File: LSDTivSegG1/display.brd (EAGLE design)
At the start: 150 x 100 mm, 95 parts, among them IC1 MEGA8-P, IC2 MAX232, IC3 PCF8574P, IC4 PCF8574P, IC5 PCF8574P, IC6 PCF8574P

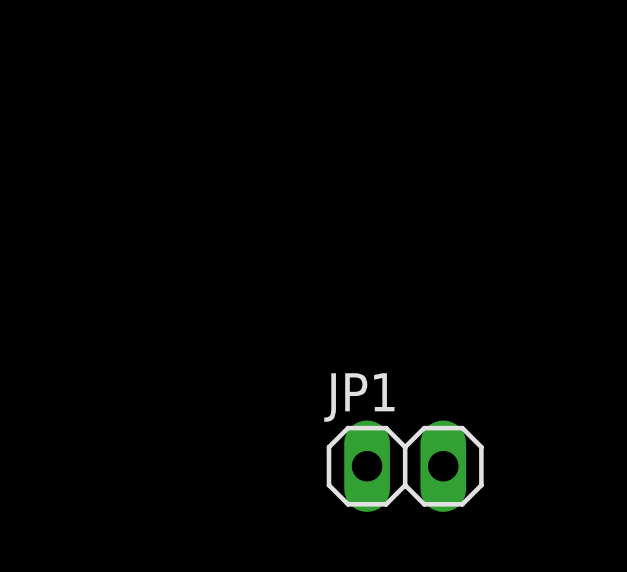
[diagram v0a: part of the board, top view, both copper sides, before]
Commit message: added RS232 crossing pinhead
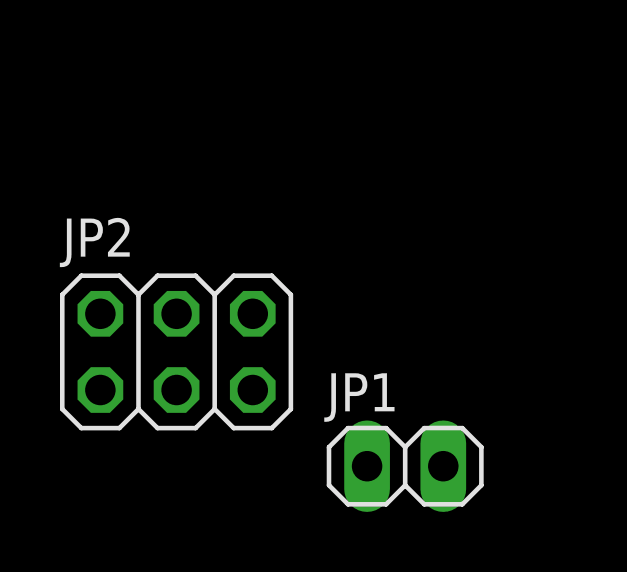
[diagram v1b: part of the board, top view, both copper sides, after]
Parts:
- added JP2: (no value), pinhead:2X03
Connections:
- new net RS232RX_CON: JP2.3, X1.2
- new net RS232TX_CON: JP2.4, X1.3
- net RS232RX: now also JP2.1, JP2.6; no longer X1.4
- net RS232TX: now also JP2.2, JP2.5; no longer X1.3
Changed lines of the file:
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@@
 <element name="U$2" library="lsd2016" package="BOARD" value="PCB" x="0" y="0"/>
 <element name="JP1" library="pinhead" library_urn="urn:adsk.eagle:library:325" package="1X02" package3d_urn="urn:adsk.eagle:package:22435/2" value="" x="-132.08" y="-5.08"/>
+<element name="JP2" library="pinhead" library_urn="urn:adsk.eagle:library:325" package="2X03" package3d_urn="urn:adsk.eagle:package:22462/2" value="" x="-139.7" y="-1.27"/>
 </elements>
 <signals>
@@
 </signal>
 <signal name="RS232TX">
-<contactref element="X1" pad="3"/>
 <contactref element="IC2" pad="13"/>
-<wire x1="-121.92" y1="96.52" x2="-29.21" y2="67.31" width="0" layer="19" extent="1-1"/>
+<contactref element="JP2" pad="5"/>
+<contactref element="JP2" pad="2"/>
+<wire x1="-137.16" y1="-2.54" x2="-142.24" y2="0" width="0" layer="19" extent="1-1"/>
+<wire x1="-121.92" y1="96.52" x2="-142.24" y2="0" width="0" layer="19" extent="1-1"/>
 </signal>
 <signal name="RS232RX">
-<contactref element="X1" pad="4"/>
 <contactref element="IC2" pad="14"/>
-<wire x1="-124.46" y1="96.52" x2="-26.4668" y2="67.31" width="0" layer="19" extent="1-1"/>
+<contactref element="JP2" pad="1"/>
+<contactref element="JP2" pad="6"/>
+<wire x1="-137.16" y1="0" x2="-142.24" y2="-2.54" width="0" layer="19" extent="1-1"/>
+<wire x1="-124.46" y1="96.52" x2="-137.16" y2="0" width="0" layer="19" extent="1-1"/>
 </signal>
 <signal name="N$1">
@@
 <wire x1="-119.38" y1="124.46" x2="-116.84" y2="88.9" width="0" layer="19" extent="1-1"/>
 </signal>
+<signal name="RS232RX_CON">
+<contactref element="X1" pad="2"/>
+<contactref element="JP2" pad="3"/>
+<wire x1="-31.9532" y1="67.31" x2="-139.7" y2="-2.54" width="0" layer="19" extent="1-1"/>
+</signal>
+<signal name="RS232TX_CON">
+<contactref element="X1" pad="3"/>
+<contactref element="JP2" pad="4"/>
+<wire x1="-29.21" y1="67.31" x2="-139.7" y2="0" width="0" layer="19" extent="1-1"/>
+</signal>
 </signals>

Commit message: added supply pins to max232
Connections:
- removed net VCC: IC2.16
- net +5V: now also IC2.16; no longer C6.-
- net GND: now also C6.-
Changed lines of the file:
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@@
 </elements>
 <signals>
-<signal name="VCC">
-<contactref element="IC2" pad="16"/>
-</signal>
 <signal name="GND">
-<contactref element="IC2" pad="15"/>
 <contactref element="C3" pad="2"/>
 <contactref element="C2" pad="2"/>
@@
 <vertex x="0" y="0"/>
 </polygon>
-<contactref element="C7" pad="+"/>
 <contactref element="SV1" pad="4"/>
 <contactref element="SV1" pad="6"/>
 <contactref element="SV1" pad="8"/>
 <contactref element="SV1" pad="10"/>
+<contactref element="C7" pad="+"/>
+<contactref element="C6" pad="-"/>
+<contactref element="IC2" pad="15"/>
 <wire x1="72.39" y1="54.61" x2="69.85" y2="62.23" width="0" layer="19" extent="1-1"/>
 <wire x1="68.58" y1="50.8" x2="72.39" y2="54.61" width="0" layer="19" extent="1-1"/>
@@
 <wire x1="-85.6488" y1="103.8606" x2="-81.9912" y2="103.8606" width="0" layer="19" extent="1-1"/>
 <wire x1="-92.1512" y1="103.8606" x2="-85.6488" y2="103.8606" width="0" layer="19" extent="1-1"/>
+<wire x1="-110.49" y1="124.46" x2="-92.1512" y2="103.8606" width="0" layer="19" extent="1-1"/>
+<wire x1="-102.87" y1="130.81" x2="-110.49" y2="124.46" width="0" layer="19" extent="1-1"/>
+<wire x1="-121.92" y1="124.46" x2="-110.49" y2="124.46" width="0" layer="19" extent="1-1"/>
 <wire x1="-127" y1="96.52" x2="-100.33" y2="88.9" width="0" layer="19" extent="1-1"/>
 <wire x1="-21.59" y1="132.08" x2="-21.0312" y2="103.8606" width="0" layer="19" extent="1-1"/>
@@
 <wire x1="-34.29" y1="132.08" x2="-27.94" y2="132.08" width="0" layer="19" extent="1-1"/>
 <wire x1="-40.64" y1="132.08" x2="-34.29" y2="132.08" width="0" layer="19" extent="1-1"/>
-<wire x1="-121.92" y1="124.46" x2="-127" y2="96.52" width="0" layer="19" extent="1-1"/>
-<wire x1="-102.87" y1="130.81" x2="-121.92" y2="124.46" width="0" layer="19" extent="1-1"/>
 <wire x1="-101.6" y1="58.42" x2="-100.33" y2="88.9" width="0" layer="19" extent="1-1"/>
 </signal>
@@
 <contactref element="R3" pad="1"/>
 <contactref element="R5" pad="2"/>
-<contactref element="C6" pad="-"/>
 <contactref element="R12" pad="2"/>
 <contactref element="R13" pad="2"/>
@@
 <contactref element="JP1" pad="2"/>
 <contactref element="SV1" pad="2"/>
+<contactref element="IC2" pad="16"/>
 <wire x1="72.39" y1="62.23" x2="74.93" y2="62.23" width="0" layer="19" extent="1-1"/>
 <wire x1="69.85" y1="54.61" x2="72.39" y2="62.23" width="0" layer="19" extent="1-1"/>
@@
 <wire x1="-105.41" y1="88.9" x2="-102.87" y2="88.9" width="0" layer="19" extent="1-1"/>
 <wire x1="-105.41" y1="96.52" x2="-105.41" y2="88.9" width="0" layer="19" extent="1-1"/>
+<wire x1="-129.54" y1="96.52" x2="-105.41" y2="96.52" width="0" layer="19" extent="1-1"/>
 <wire x1="-99.06" y1="58.42" x2="-72.39" y2="67.31" width="0" layer="19" extent="1-1"/>
-<wire x1="-110.49" y1="124.46" x2="-105.41" y2="96.52" width="0" layer="19" extent="1-1"/>
-<wire x1="-113.03" y1="130.81" x2="-110.49" y2="124.46" width="0" layer="19" extent="1-1"/>
-<wire x1="-114.3" y1="137.16" x2="-113.03" y2="130.81" width="0" layer="19" extent="1-1"/>
-<wire x1="-114.3" y1="142.24" x2="-114.3" y2="137.16" width="0" layer="19" extent="1-1"/>
-<wire x1="-102.87" y1="130.81" x2="-110.49" y2="124.46" width="0" layer="19" extent="1-1"/>
+<wire x1="-102.87" y1="130.81" x2="-105.41" y2="96.52" width="0" layer="19" extent="1-1"/>
 <wire x1="-104.14" y1="137.16" x2="-102.87" y2="130.81" width="0" layer="19" extent="1-1"/>
 <wire x1="-104.14" y1="142.24" x2="-104.14" y2="137.16" width="0" layer="19" extent="1-1"/>
@@
 <wire x1="-12.7" y1="147.32" x2="-22.86" y2="147.32" width="0" layer="19" extent="1-1"/>
 <wire x1="-12.7" y1="142.24" x2="-12.7" y2="147.32" width="0" layer="19" extent="1-1"/>
+<wire x1="-114.3" y1="142.24" x2="-104.14" y2="142.24" width="0" layer="19" extent="1-1"/>
+<wire x1="-114.3" y1="137.16" x2="-114.3" y2="142.24" width="0" layer="19" extent="1-1"/>
+<wire x1="-113.03" y1="130.81" x2="-114.3" y2="137.16" width="0" layer="19" extent="1-1"/>
 <wire x1="-124.46" y1="142.24" x2="-114.3" y2="142.24" width="0" layer="19" extent="1-1"/>
 <wire x1="-124.46" y1="137.16" x2="-124.46" y2="142.24" width="0" layer="19" extent="1-1"/>
@@
 <wire x1="-92.71" y1="124.46" x2="-124.46" y2="88.9" width="0" layer="19" extent="1-1"/>
 </signal>
-<signal name="N$7">
-<contactref element="IC2" pad="2"/>
-<contactref element="C6" pad="+"/>
-<wire x1="-113.03" y1="124.46" x2="-127" y2="88.9" width="0" layer="19" extent="1-1"/>
-</signal>
 <signal name="N$15">
 <contactref element="R12" pad="1"/>
@@
 <wire x1="-25.0952" y1="69.85" x2="-133.35" y2="-5.08" width="0" layer="19" extent="1-1"/>
 </signal>
+<signal name="RS232RX_CON">
+<contactref element="X1" pad="2"/>
+<contactref element="JP2" pad="3"/>
+<wire x1="-31.9532" y1="67.31" x2="-139.7" y2="-2.54" width="0" layer="19" extent="1-1"/>
+</signal>
+<signal name="RS232TX_CON">
+<contactref element="X1" pad="3"/>
+<contactref element="JP2" pad="4"/>
+<wire x1="-29.21" y1="67.31" x2="-139.7" y2="0" width="0" layer="19" extent="1-1"/>
+</signal>
+<signal name="N$7">
+<contactref element="IC2" pad="2"/>
+<contactref element="C6" pad="+"/>
+<wire x1="-113.03" y1="124.46" x2="-127" y2="88.9" width="0" layer="19" extent="1-1"/>
+</signal>
 <signal name="N$8">
 <contactref element="IC2" pad="6"/>
@@
 <wire x1="-119.38" y1="124.46" x2="-116.84" y2="88.9" width="0" layer="19" extent="1-1"/>
 </signal>
-<signal name="RS232RX_CON">
-<contactref element="X1" pad="2"/>
-<contactref element="JP2" pad="3"/>
-<wire x1="-31.9532" y1="67.31" x2="-139.7" y2="-2.54" width="0" layer="19" extent="1-1"/>
-</signal>
-<signal name="RS232TX_CON">
-<contactref element="X1" pad="3"/>
-<contactref element="JP2" pad="4"/>
-<wire x1="-29.21" y1="67.31" x2="-139.7" y2="0" width="0" layer="19" extent="1-1"/>
-</signal>
 </signals>

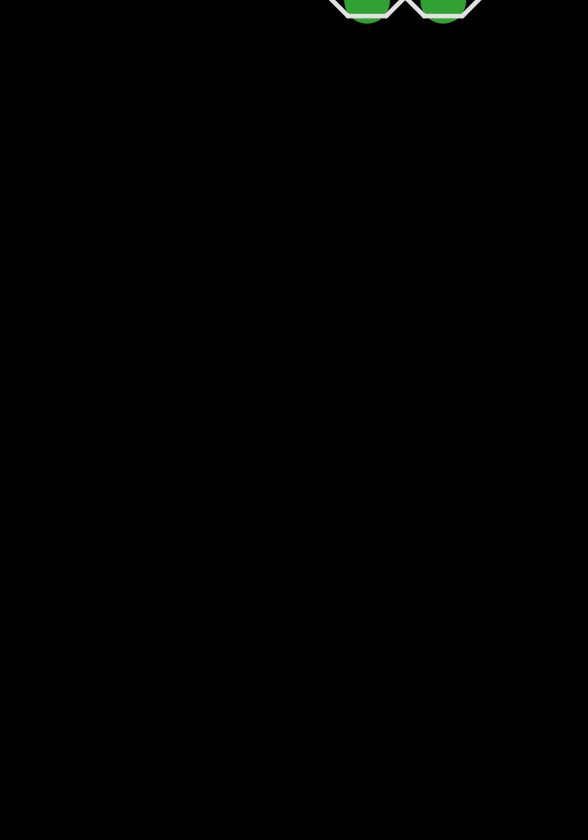
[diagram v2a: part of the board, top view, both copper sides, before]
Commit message: added blocking capacities to IO-Expanders
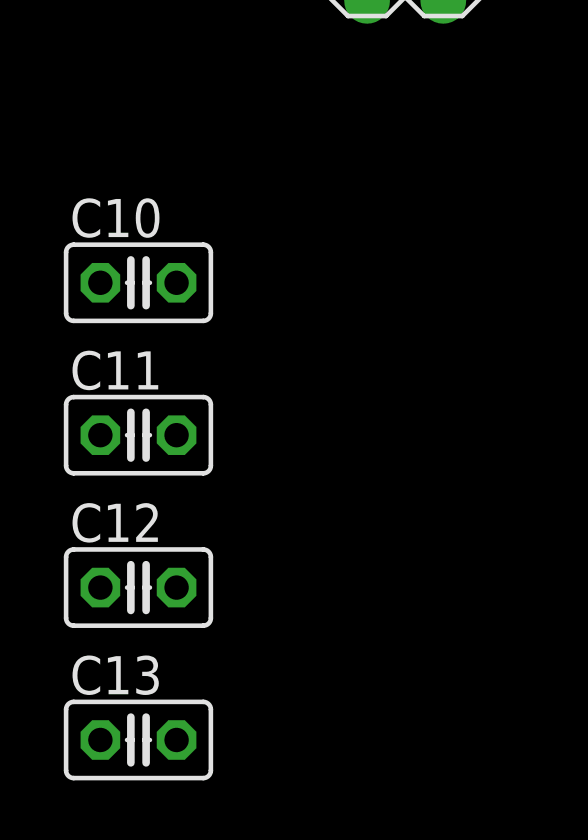
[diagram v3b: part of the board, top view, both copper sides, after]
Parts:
- added C10, C11, C12, C13: (no value), rcl:C025-025X050
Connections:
- net +5V: now also C10.1, C11.1, C12.1, C13.1
- net GND: now also C10.2, C11.2, C12.2, C13.2

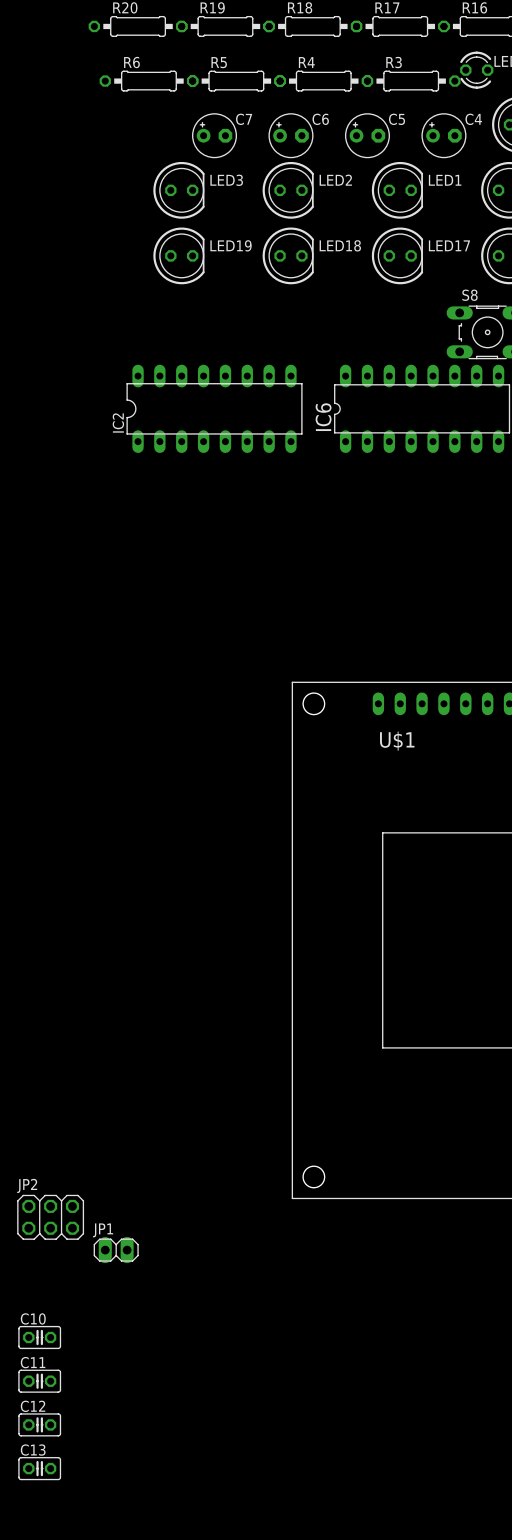
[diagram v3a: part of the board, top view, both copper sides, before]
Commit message: updated display contrast trimming circuit
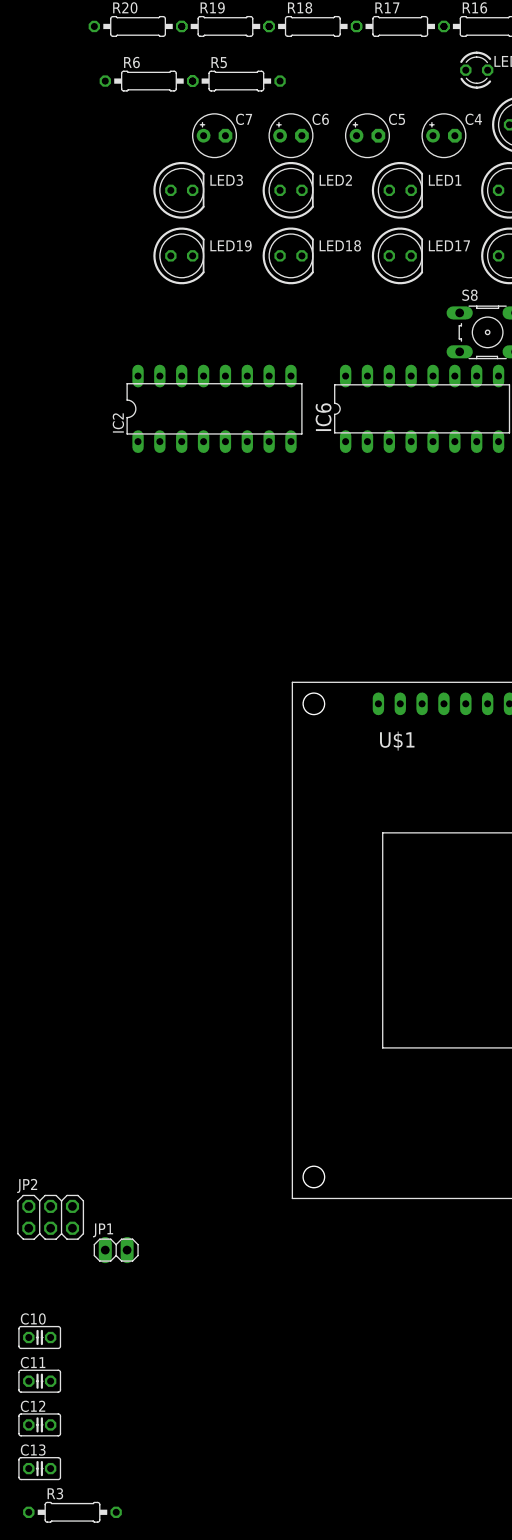
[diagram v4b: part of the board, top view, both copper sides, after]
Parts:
- removed R4: 1k0, rcl:0207/10
- R2: value 10k -> 5k
- R3: value 2k2 -> 15k
- moved R3 171.0 mm to (-137.2, -35.6)
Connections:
- net +5V: now also R2.A, U$1.1, U$1.16
- net GND: no longer R2.A, R4.2, U$1.1, U$1.16
- net N$9: no longer R4.1

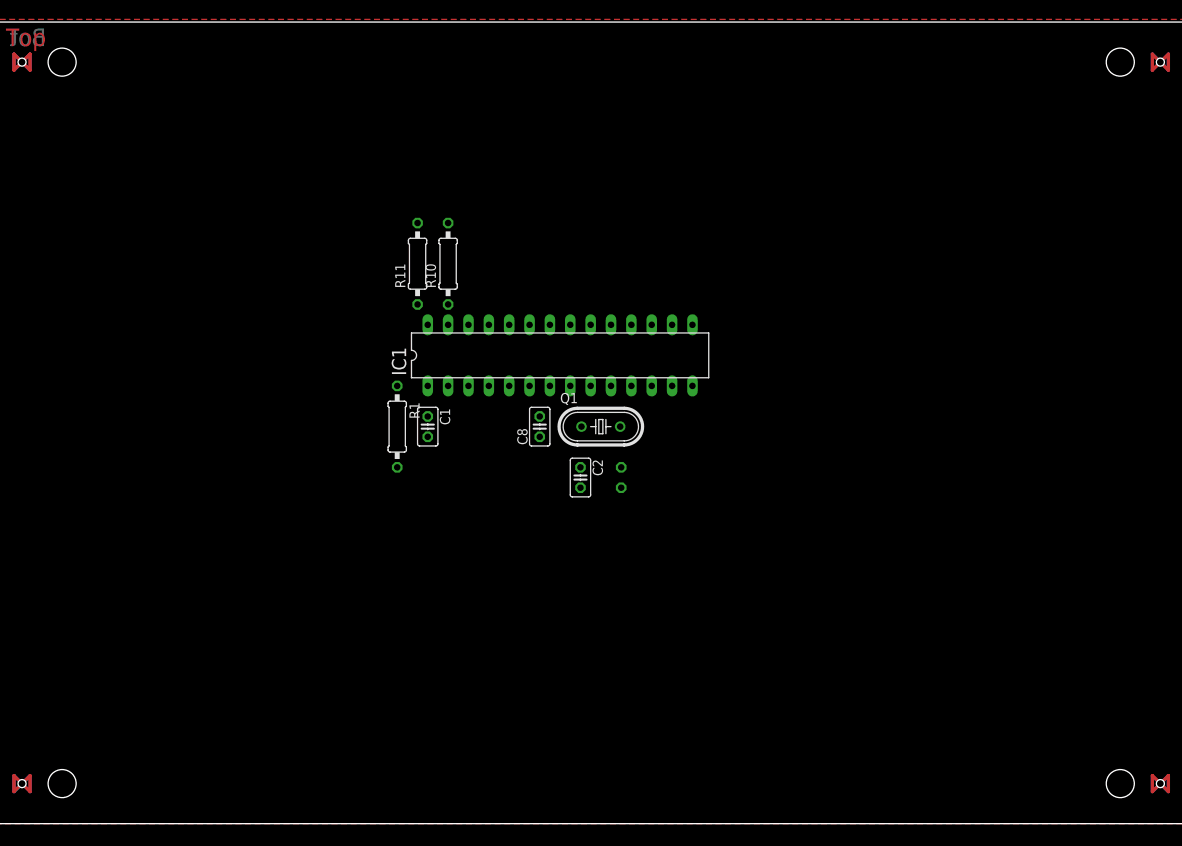
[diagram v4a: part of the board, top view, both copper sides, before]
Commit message: added display board frame to library replaced board frame in display schematic
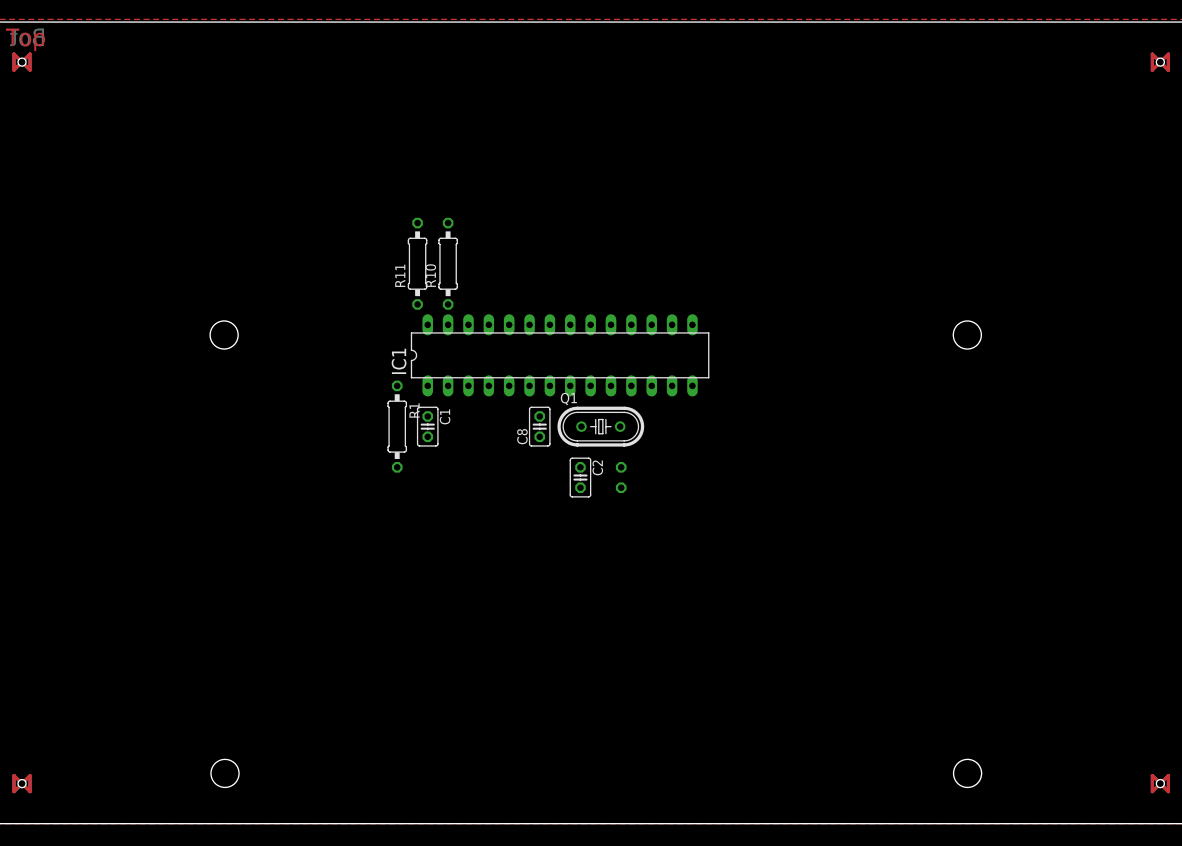
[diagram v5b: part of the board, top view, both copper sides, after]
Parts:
- U$2: value PCB -> DISPLAY_FRAME; device lsd2016:BOARD -> lsd2016:DISPLAY_FRAME
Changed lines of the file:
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@@
 <attribute name="OC_NEWARK" value="unknown" x="-29.21" y="68.58" size="1.778" layer="27" display="off"/>
 </element>
-<element name="U$2" library="lsd2016" package="BOARD" value="PCB" x="0" y="0"/>
 <element name="JP1" library="pinhead" library_urn="urn:adsk.eagle:library:325" package="1X02" package3d_urn="urn:adsk.eagle:package:22435/2" value="" x="-132.08" y="-5.08"/>
 <element name="JP2" library="pinhead" library_urn="urn:adsk.eagle:library:325" package="2X03" package3d_urn="urn:adsk.eagle:package:22462/2" value="" x="-139.7" y="-1.27"/>
@@
 <attribute name="SPICEPREFIX" value="R" x="-137.16" y="-35.56" size="1.778" layer="27" display="off"/>
 </element>
+<element name="U$2" library="lsd2016" package="DISPLAY_FRAME" value="DISPLAY_FRAME" x="0" y="0"/>
 </elements>
 <signals>

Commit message: added values to PCF blocking capacities
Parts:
- C10, C11, C12, C13: value (none) -> 100nF
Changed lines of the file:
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@@
 <element name="JP1" library="pinhead" library_urn="urn:adsk.eagle:library:325" package="1X02" package3d_urn="urn:adsk.eagle:package:22435/2" value="" x="-132.08" y="-5.08"/>
 <element name="JP2" library="pinhead" library_urn="urn:adsk.eagle:library:325" package="2X03" package3d_urn="urn:adsk.eagle:package:22462/2" value="" x="-139.7" y="-1.27"/>
-<element name="C10" library="rcl" library_urn="urn:adsk.eagle:library:334" package="C025-025X050" package3d_urn="urn:adsk.eagle:package:23629/2" value="" x="-140.97" y="-15.24">
+<element name="C10" library="rcl" library_urn="urn:adsk.eagle:library:334" package="C025-025X050" package3d_urn="urn:adsk.eagle:package:23629/2" value="100nF" x="-140.97" y="-15.24">
 <attribute name="SPICEPREFIX" value="C" x="-140.97" y="-15.24" size="1.778" layer="27" display="off"/>
 </element>
-<element name="C11" library="rcl" library_urn="urn:adsk.eagle:library:334" package="C025-025X050" package3d_urn="urn:adsk.eagle:package:23629/2" value="" x="-140.97" y="-20.32">
+<element name="C11" library="rcl" library_urn="urn:adsk.eagle:library:334" package="C025-025X050" package3d_urn="urn:adsk.eagle:package:23629/2" value="100nF" x="-140.97" y="-20.32">
 <attribute name="SPICEPREFIX" value="C" x="-140.97" y="-20.32" size="1.778" layer="27" display="off"/>
 </element>
-<element name="C12" library="rcl" library_urn="urn:adsk.eagle:library:334" package="C025-025X050" package3d_urn="urn:adsk.eagle:package:23629/2" value="" x="-140.97" y="-25.4">
+<element name="C12" library="rcl" library_urn="urn:adsk.eagle:library:334" package="C025-025X050" package3d_urn="urn:adsk.eagle:package:23629/2" value="100nF" x="-140.97" y="-25.4">
 <attribute name="SPICEPREFIX" value="C" x="-140.97" y="-25.4" size="1.778" layer="27" display="off"/>
 </element>
-<element name="C13" library="rcl" library_urn="urn:adsk.eagle:library:334" package="C025-025X050" package3d_urn="urn:adsk.eagle:package:23629/2" value="" x="-140.97" y="-30.48">
+<element name="C13" library="rcl" library_urn="urn:adsk.eagle:library:334" package="C025-025X050" package3d_urn="urn:adsk.eagle:package:23629/2" value="100nF" x="-140.97" y="-30.48">
 <attribute name="SPICEPREFIX" value="C" x="-140.97" y="-30.48" size="1.778" layer="27" display="off"/>
 </element>
